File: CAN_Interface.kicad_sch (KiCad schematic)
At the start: 0 parts

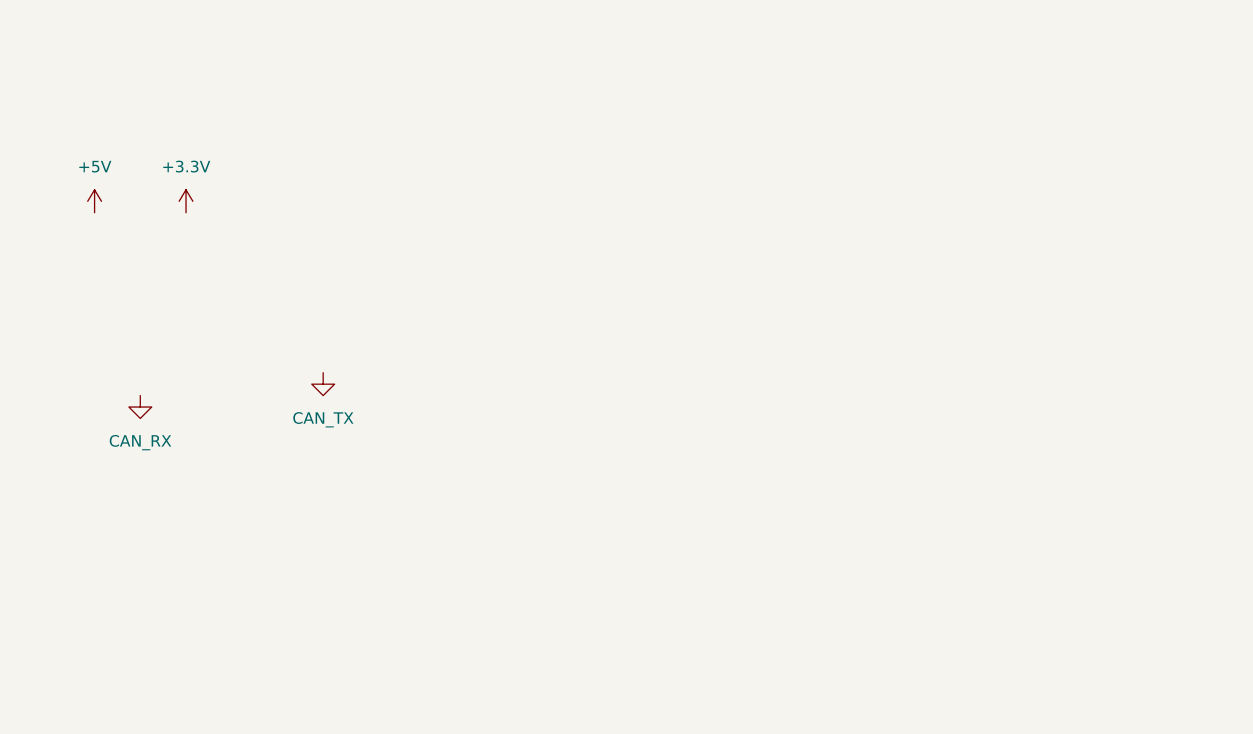
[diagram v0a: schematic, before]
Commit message: Connected the three supplies (Vcc, Vio, Vsup) to the power supply via 5V. Added a terminating node for the CANH and CANL. Need to reassign pins for GPIO, TX and RX.
Signed-off-by: Emily <124216516+epariag@users.noreply.github.com>
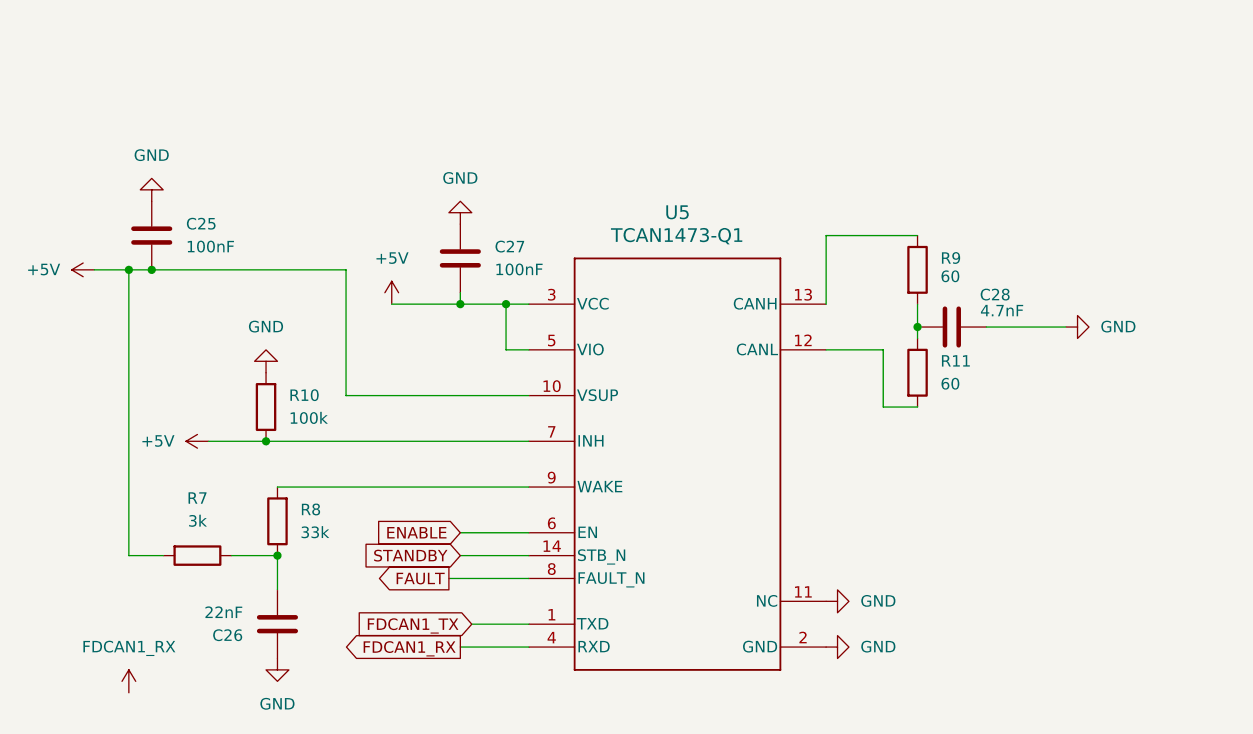
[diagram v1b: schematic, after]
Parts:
- added C25, C27: 100nF, Capacitor_SMD:C_0402_1005Metric, symbol Device:C
- added C26: 22nF, Capacitor_SMD:C_0402_1005Metric, symbol Device:C
- added C28: 4.7nF, Capacitor_SMD:C_0402_1005Metric, symbol Device:C
- added R10: 100k, symbol Device:R
- added R11, R9: 60, symbol Device:R
- added R7: 3k, Resistor_SMD:R_0402_1005Metric, symbol Device:R
- added R8: 33k, Resistor_SMD:R_0402_1005Metric, symbol Device:R
- added U5: TCAN1473-Q1, footprints:D0014A-IPC_B, symbol 2026-07-01_00-05-57:PTCAN1473DRQ1
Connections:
- net +5V: now also C25.1, C27.1, R10.1, R7.2, U5.10 (VSUP), U5.3 (VCC), U5.5 (VIO), U5.7 (INH)
- new net: R9.1, U5.13 (CANH)
- new net: C28.2, R11.1, R9.2
- new net: R11.2, U5.12 (CANL)
- new net: C26.1, R7.1, R8.1
- new net: R8.2, U5.9 (WAKE)
- new net ENABLE: U5.6 (EN)
- new net FAULT: U5.8 (FAULT_N)
- new net FDCAN1_RX: U5.4 (RXD)
- new net FDCAN1_TX: U5.1 (TXD)
- new net GND: C25.2, C26.2, C27.2, C28.1, R10.2, U5.11 (NC), U5.2 (GND)
- new net STANDBY: U5.14 (STB_N)

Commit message: Added filter, transient and ESD based on application diagram. Changed global labels to rails.
Signed-off-by: Emily <124216516+epariag@users.noreply.github.com>
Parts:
- added C29, C30: 100n, Capacitor_SMD:C_0402_1005Metric, symbol Device:C
- added D3, D4: SMBJ15A, symbol Device:D_TVS
- C25, C27: value 100nF -> 100n
- C26: value 22nF -> 22n
- C28: value 4.7nF -> 4.7n
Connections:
- net FDCAN1_RX: now also U5.1 (TXD); no longer U5.4 (RXD)
- net FDCAN1_TX: now also U5.4 (RXD); no longer U5.1 (TXD)
- net GND: now also C29.1, C30.1, D3.2 (A2), D4.1 (A1)
- net at R9.1, U5.13 (CANH): now also C30.2, D3.1 (A1)
- net at R11.2, U5.12 (CANL): now also C29.2, D4.2 (A2)

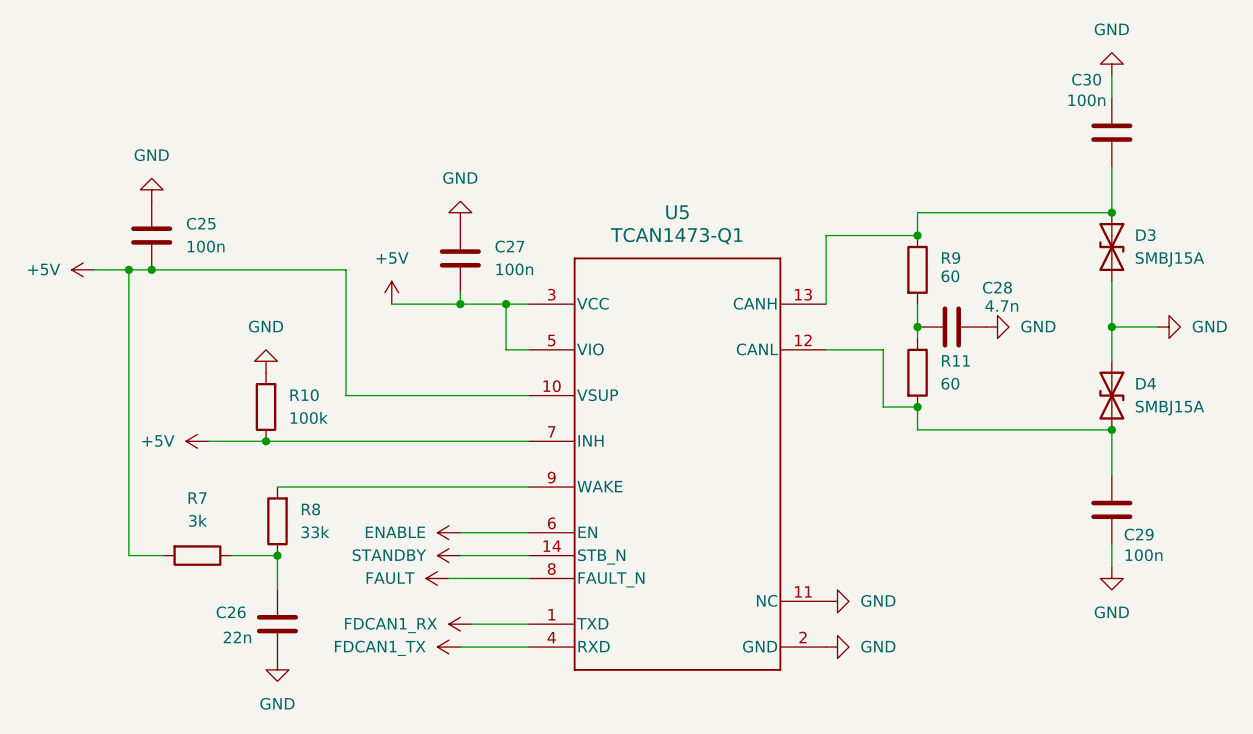
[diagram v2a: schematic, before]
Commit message: .Removed INH connection. Changed voltage of Vio to 3.3V. Assigned footprintd for CAN_interface components.
Signed-off-by: Emily <124216516+epariag@users.noreply.github.com>
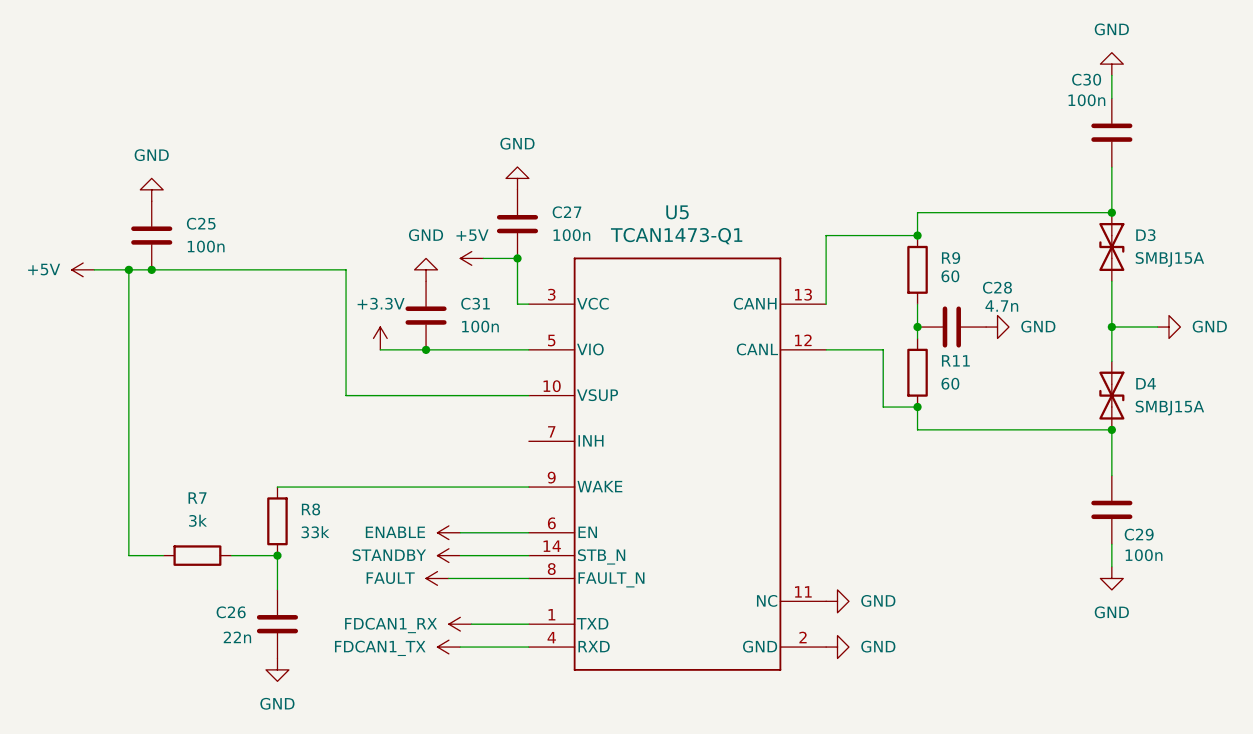
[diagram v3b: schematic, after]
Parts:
- removed R10: 100k, symbol Device:R
- added C31: 100n, Capacitor_SMD:C_0402_1005Metric, symbol Device:C
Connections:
- net +5V: no longer U5.5 (VIO), U5.7 (INH)
- net GND: now also C31.2
- new net +3.3V: C31.1, U5.5 (VIO)
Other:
- moved on the sheet: C27
